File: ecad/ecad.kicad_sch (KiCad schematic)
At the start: 19 parts, among them J1 Raspberry_Pi_2_3, Q1 BC547, Q4 BC547, SW1 Power Button, U2 USB PD/QC Decoy, U6 Power Bank

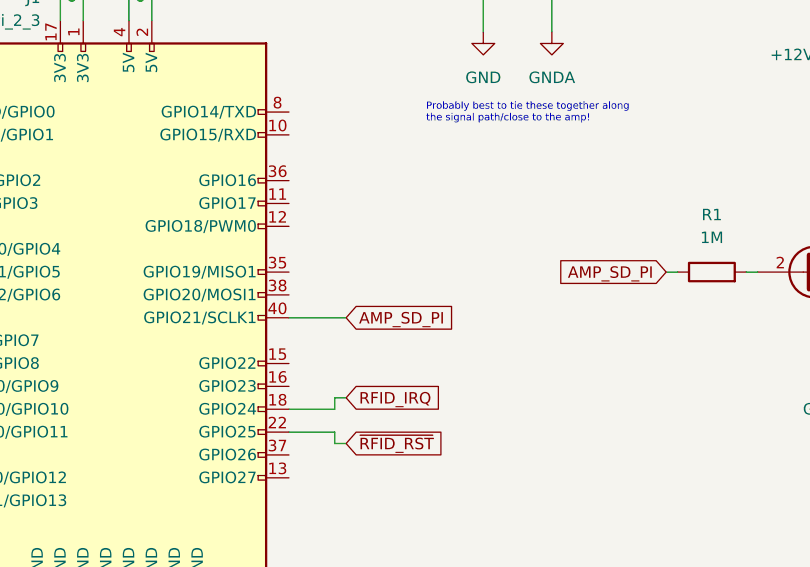
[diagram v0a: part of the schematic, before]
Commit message: update schematic for amp power ctl
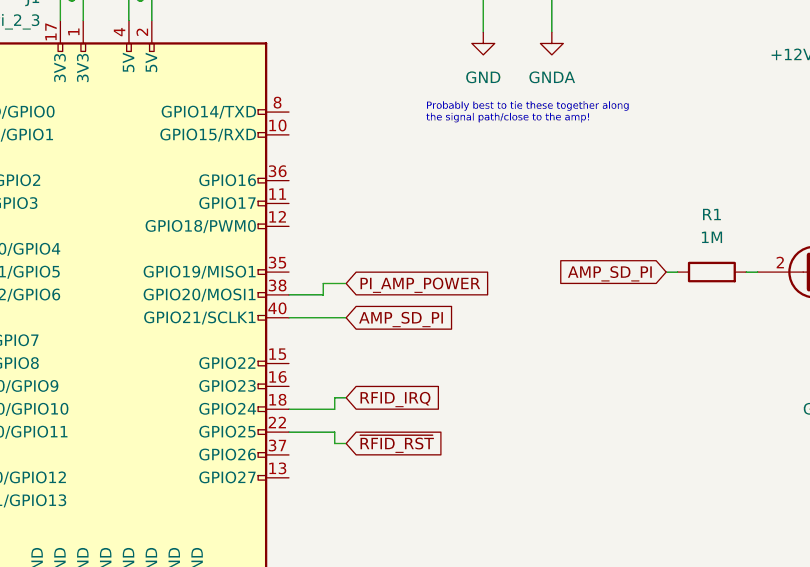
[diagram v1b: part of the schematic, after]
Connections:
- net PI_AMP_POWER: now also J1.38 (GPIO20/MOSI1)
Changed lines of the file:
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@@
+    (stroke (width 0) (type default))
+  )
+  (wire (pts (xy 114.3 132.08) (xy 118.11 132.08))
     (stroke (width 0) (type default))
   )
@@
     (stroke (width 0) (type default))
   )
+  (wire (pts (xy 118.11 130.81) (xy 120.65 130.81))
+    (stroke (width 0) (type default))
+  )
   (wire (pts (xy 182.88 111.76) (xy 182.88 116.84))
     (stroke (width 0) (type default))
@@
   )
   (wire (pts (xy 66.04 59.69) (xy 66.04 62.23))
+    (stroke (width 0) (type default))
+  )
+  (wire (pts (xy 118.11 132.08) (xy 118.11 130.81))
     (stroke (width 0) (type default))
   )
@@
     )
   )
+  (global_label "PI_AMP_POWER" (shape input) (at 120.65 130.81 0) (fields_autoplaced)
+    (effects (font (size 1.27 1.27)) (justify left))
+    (property "Intersheetrefs" "${INTERSHEET_REFS}" (at 137.7261 130.81 0)
+      (effects (font (size 1.27 1.27)) (justify left) hide)
+    )
+  )

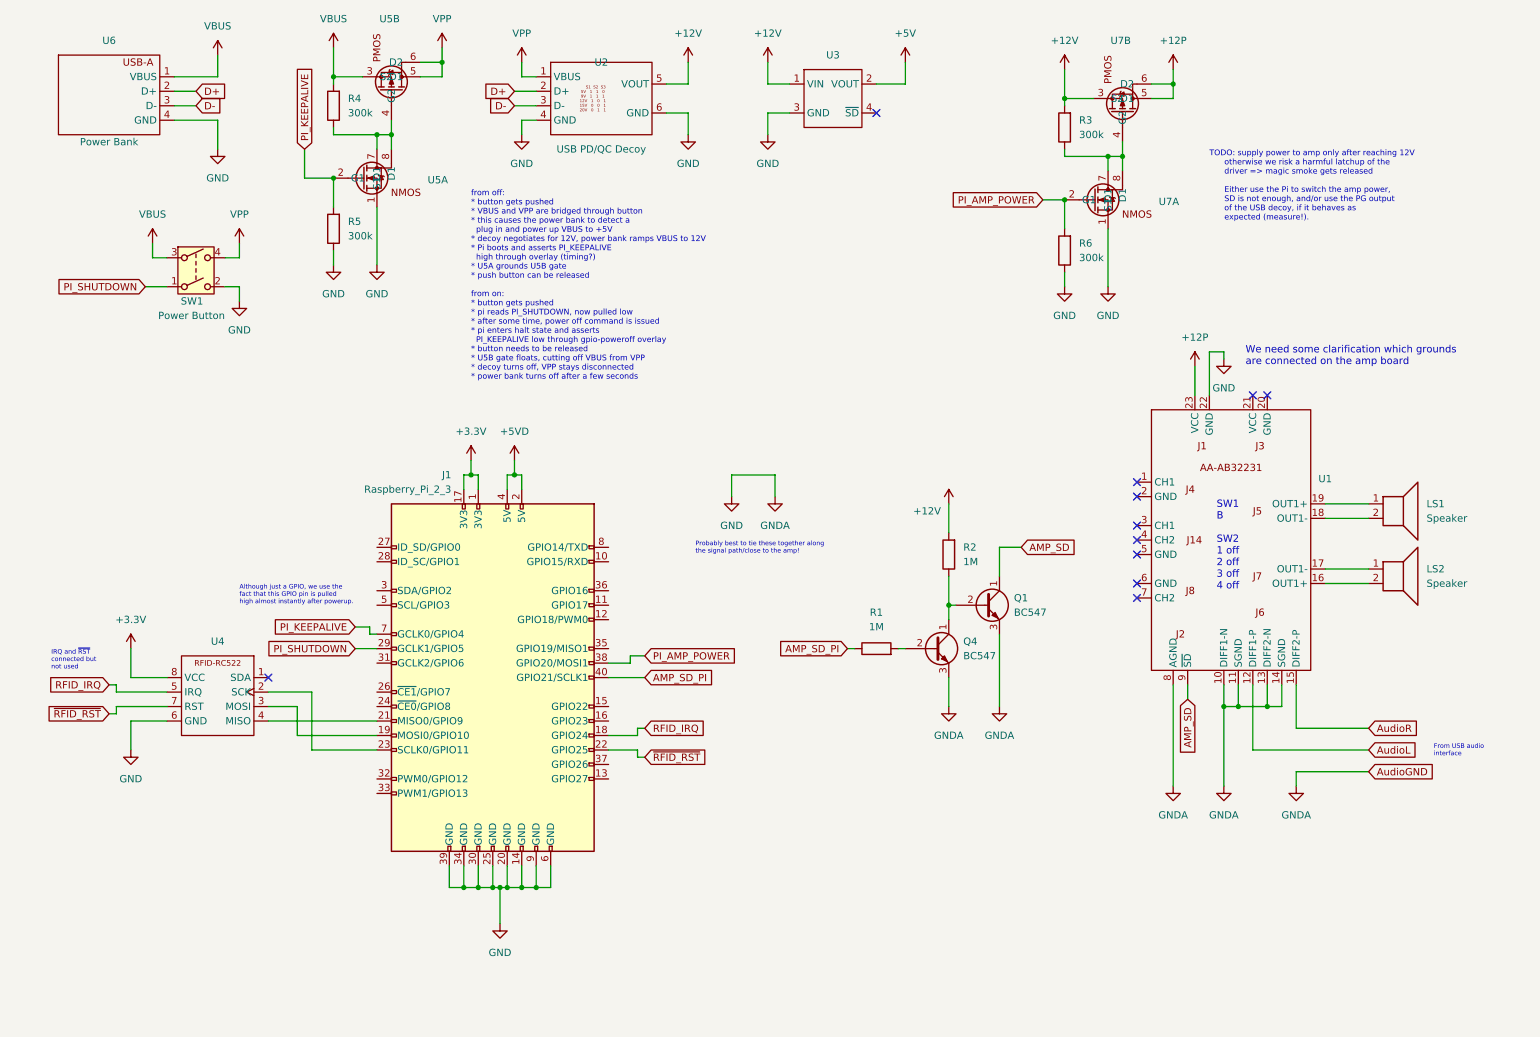
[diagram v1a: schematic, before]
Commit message: Replaced step-down with DC/DC converter and added digital grounds
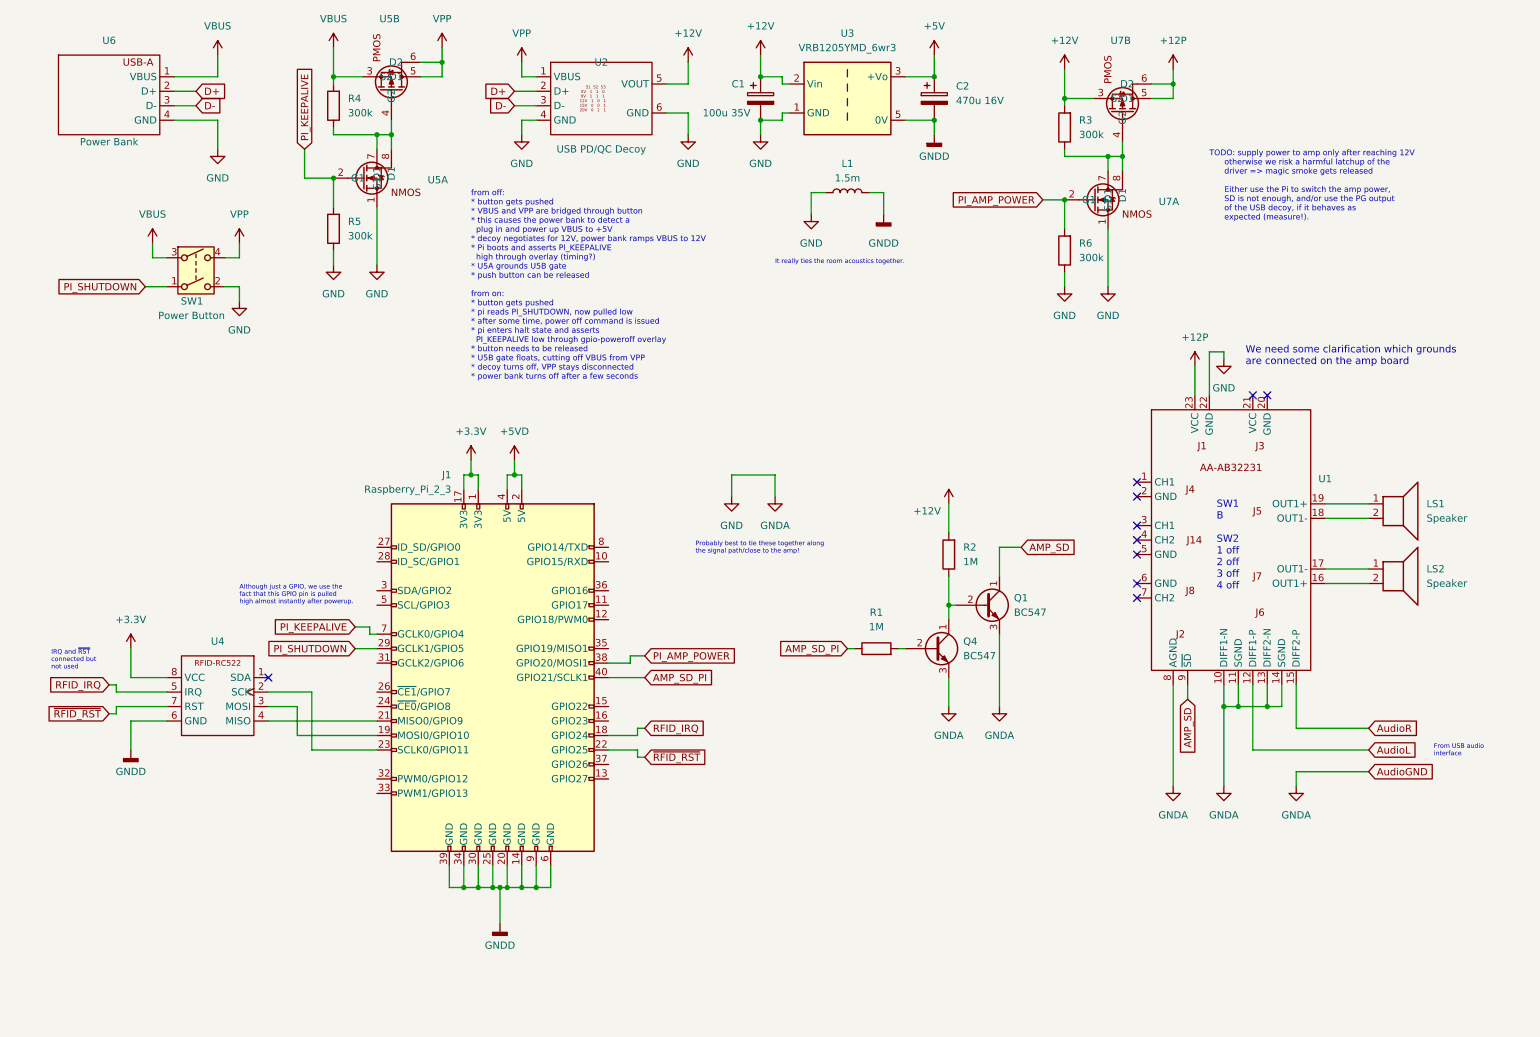
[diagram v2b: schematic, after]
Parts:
- removed U3: ~, symbol drempelbox:5V_Buck
- added C1: 100u 35V, symbol Device:C_Polarized
- added C2: 470u 16V, symbol Device:C_Polarized
- added L1: 1.5m, symbol Device:L
- added U3: VRB1205YMD_6wr3, Converter_DCDC:Converter_DCDC_MORNSUN_VRBxxxxYMD_6WR3_Single, symbol drempelbox:VRB1205YMD_6wr3
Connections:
- net +12V: now also C1.1, U3.2 (Vin)
- net +5V: now also C2.1, U3.3 (+Vo)
- net GND: now also C1.2, L1.1, U3.1 (GND); no longer J1.14 (GND), J1.20 (GND), J1.25 (GND), J1.30 (GND), J1.34 (GND), J1.39 (GND), J1.6 (GND), J1.9 (GND), U4.6 (GND)
- new net GNDD: C2.2, J1.14 (GND), J1.20 (GND), J1.25 (GND), J1.30 (GND), J1.34 (GND), J1.39 (GND), J1.6 (GND), J1.9 (GND), L1.2, U3.5 (0V), U4.6 (GND)
- no-connect marks 11 -> 10
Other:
- note added: "It really ties the room acoustics together."

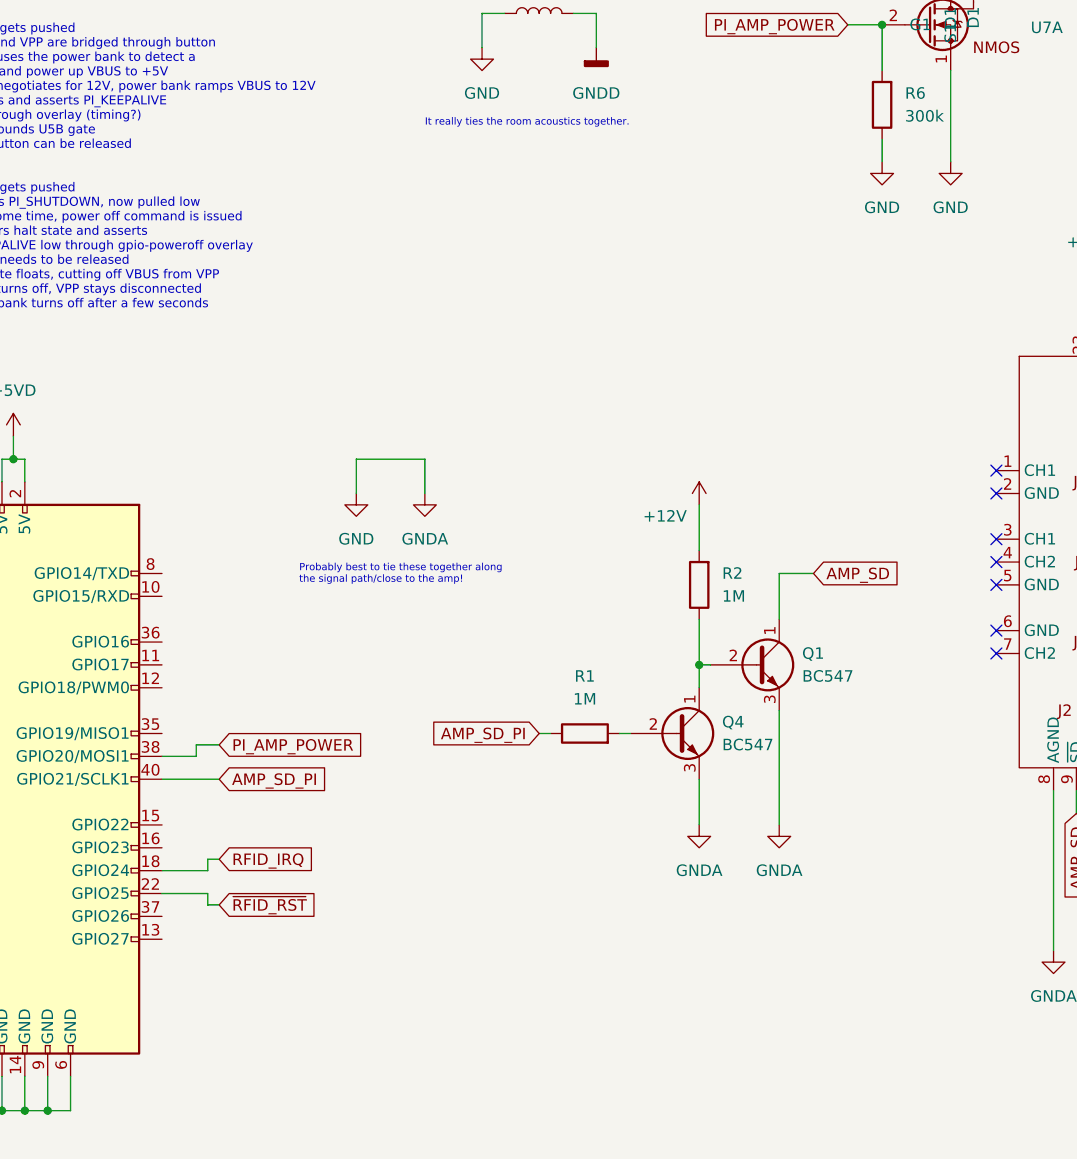
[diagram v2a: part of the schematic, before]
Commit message: Added volume buttons.
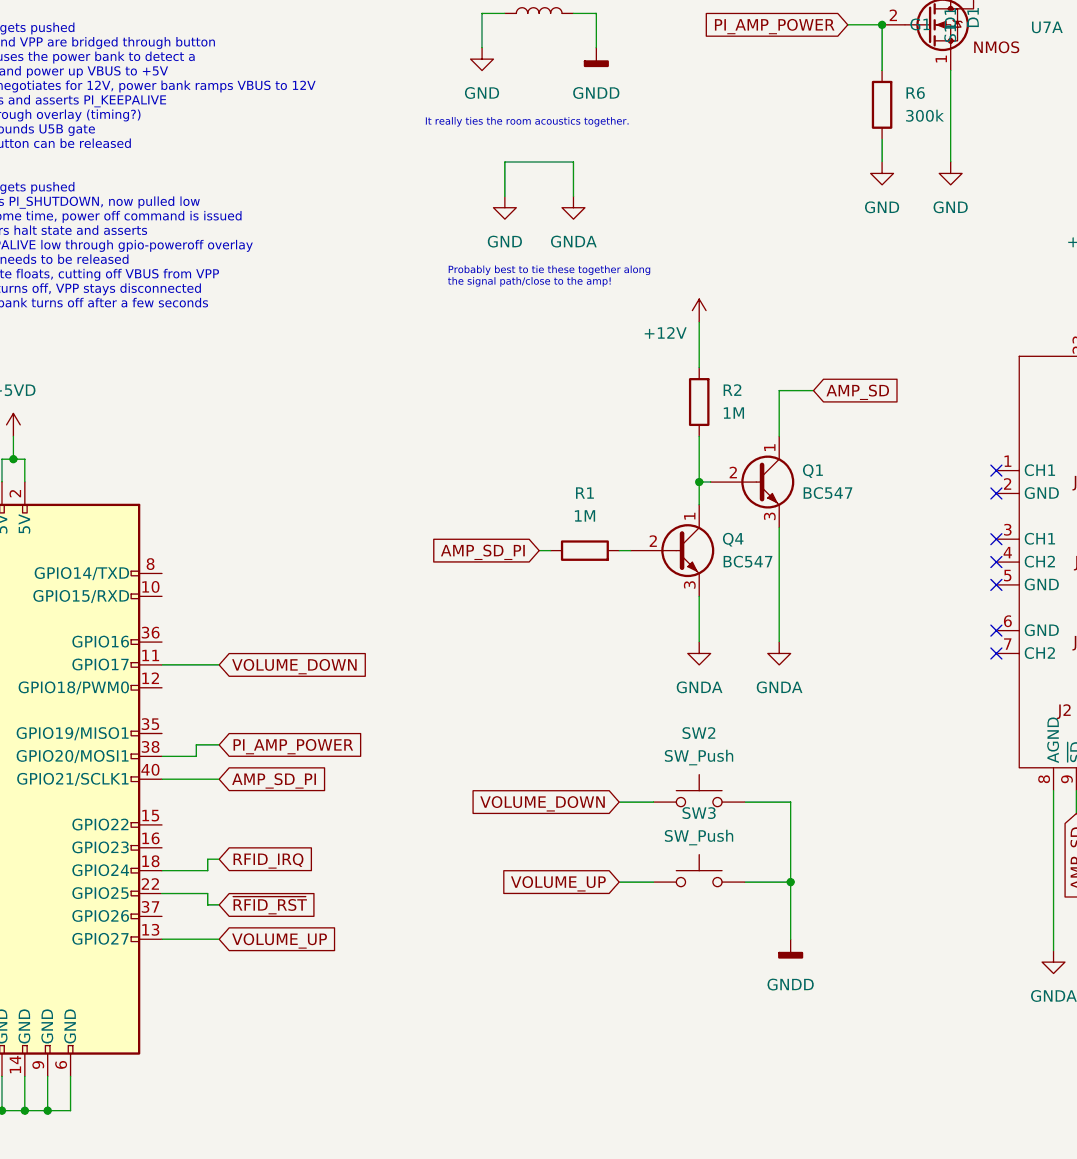
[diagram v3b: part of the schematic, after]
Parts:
- added SW2, SW3: SW_Push, symbol Switch:SW_Push
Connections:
- net GNDD: now also SW2.2, SW3.2
- net VOLUME_DOWN: now reaches J1.11 (GPIO17)
- net VOLUME_DOWN: now also SW2.1
- net VOLUME_UP: now reaches J1.13 (GPIO27)
- net VOLUME_UP: now also SW3.1
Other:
- moved on the sheet: Q1, Q4, R1, R2

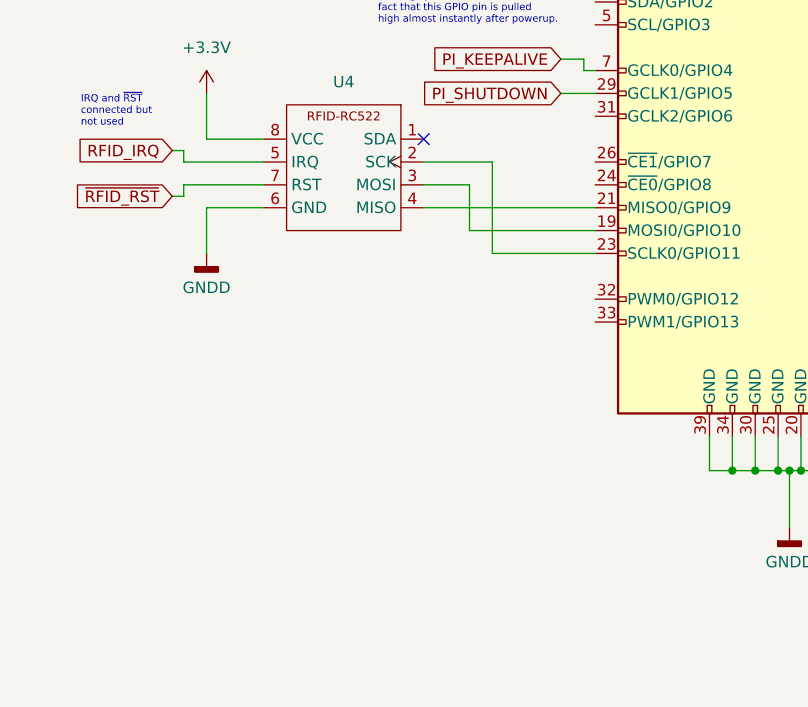
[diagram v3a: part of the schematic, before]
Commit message: Added status LED circuit.
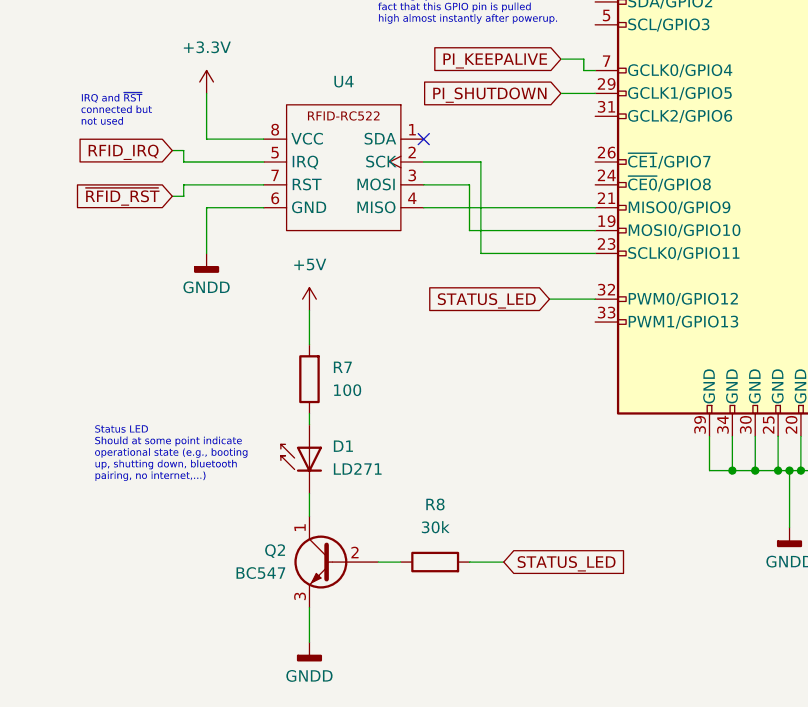
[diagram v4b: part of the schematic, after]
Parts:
- added D1: LD271, LED_THT:LED_D5.0mm_IRGrey, symbol LED:LD271
- added Q2: BC547, Package_TO_SOT_THT:TO-92_Inline, symbol Transistor_BJT:BC547
- added R7: 100, symbol Device:R
- added R8: 30k, symbol Device:R
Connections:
- net +5V: now also R7.2
- net GNDD: now also Q2.3 (E)
- net STATUS_LED: now reaches J1.32 (PWM0/GPIO12)
- net STATUS_LED: now also R8.2
- new net: D1.1 (K), Q2.1 (C)
- new net: D1.2 (A), R7.1
- new net: Q2.2 (B), R8.1
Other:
- note added: "Status LED Should at some point indicate operational state (e.g., booting up, shutting down, bluetooth pairing, no internet,...)"

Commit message: Some annotations.
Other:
- note added: "Assuming white LED with 4V/10mA flux voltage and current"
- note added: "Couldn't find a Wald&Wiesen LED in the library..."
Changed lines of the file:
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@@
+		)
+	)
+	(text "Couldn't find a\nWald&Wiesen LED\nin the library..."
+		(exclude_from_sim no)
+		(at 51.308 171.704 0)
+		(effects
+			(font
+				(size 0.8 0.8)
+			)
+			(justify left bottom)
 		)
 	)
@@
 		(effects
 			(font
+				(size 0.8 0.8)
+			)
+			(justify left bottom)
+		)
+	)
+	(text "Assuming white LED\nwith 4V/10mA flux\nvoltage and current"
+		(exclude_from_sim no)
+		(at 48.514 162.814 0)
+		(effects
+			(font
